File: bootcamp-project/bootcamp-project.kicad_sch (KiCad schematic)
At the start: 17 parts, among them J3 FTDI, SW1 SW_Push, U1 ATmega328P-A, Y1 16MHz

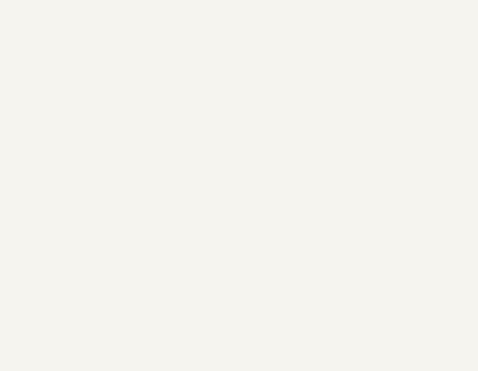
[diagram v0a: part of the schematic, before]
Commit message: lib: fix power flag, foot: add jumpers
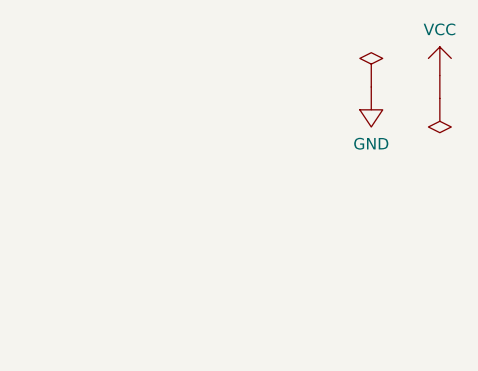
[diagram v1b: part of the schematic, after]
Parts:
- added U2, U3: ~, symbol bootcamp00:POWER_FLAG

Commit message: lib: fix schematic with power flags
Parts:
- added U10, U11, U12, U13, U4, U5, U6, U7, U8, U9: ~, symbol bootcamp00:POWER_FLAG
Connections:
- net RAW: now also U2.1
- net at U1.18 (AVCC), U1.4 (VCC): now also U1.6, U10.1
- net at U1.3 (GND): now also U1.21, U1.5, U13.1
- net at C3.0: now also U9.1
- net at R3.0: now also U4.1
- net at D1.1: now also U6.1
- net at C1.1, C2.1, Y1.2: now also U11.1
- net at Y1.4: now also U12.1
- net at C4.0: now also U5.1
- net at C6.1: now also U8.1
- net at R2.1: now also U3.1
- net at C7.1: now also U7.1

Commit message: sche: update schematic'
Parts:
- C1, C2, C3, C4, C6, C7: footprint (none) -> Library:marge_capacitor
- D1, D2: footprint (none) -> Library:marge_led
- J1: footprint (none) -> Library:JUMPER_12_J1
- J2: footprint (none) -> Library:JUMPER_12_J2
- J3: footprint (none) -> Library:JUMPER_FDTI
- R1, R2, R3: footprint (none) -> Library:marge_resistor
- SW1: footprint (none) -> Library:SWITCH_SW
- U1: footprint (none) -> Library:ATMEGA328p
- Y1: footprint (none) -> Library:QUARTZ_16MHz
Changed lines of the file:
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@@
 			)
 		)
-		(property "Footprint" ""
+		(property "Footprint" "Library:ATMEGA328p"
 			(at 81.28 177.8 0)
 			(effects
@@
 			)
 		)
-		(property "Footprint" ""
+		(property "Footprint" "Library:marge_capacitor"
 			(at 40.64 104.14 0)
 			(effects
@@
 			)
 		)
-		(property "Footprint" ""
+		(property "Footprint" "Library:marge_resistor"
 			(at 205.74 43.18 0)
 			(effects
@@
 			)
 		)
-		(property "Footprint" ""
+		(property "Footprint" "Library:marge_led"
 			(at 135.89 44.45 0)
 			(effects
@@
 	)
 	(symbol
-		(lib_name "POWER_FLAG_2")
 		(lib_id "bootcamp00:POWER_FLAG")
 		(at 205.74 36.83 90)
@@
 			)
 		)
-		(property "Footprint" ""
+		(property "Footprint" "Library:QUARTZ_16MHz"
 			(at 106.68 130.81 0)
 			(effects
@@
 			)
 		)
-		(property "Footprint" ""
+		(property "Footprint" "Library:marge_resistor"
 			(at 134.62 31.75 0)
 			(effects
@@
 			)
 		)
-		(property "Footprint" ""
+		(property "Footprint" "Library:marge_capacitor"
 			(at 185.42 48.26 0)
 			(effects
@@
 			)
 		)
-		(property "Footprint" ""
+		(property "Footprint" "Library:marge_capacitor"
 			(at 43.18 39.37 0)
 			(effects
@@
 			)
 		)
-		(property "Footprint" ""
+		(property "Footprint" "Library:marge_capacitor"
 			(at 115.57 134.62 0)
 			(effects
@@
 	)
 	(symbol
-		(lib_name "POWER_FLAG_1")
 		(lib_id "bootcamp00:POWER_FLAG")
 		(at 63.5 52.07 90)
@@
 	)
 	(symbol
-		(lib_name "POWER_FLAG_3")
 		(lib_id "bootcamp00:POWER_FLAG")
 		(at 175.26 53.34 270)
@@
 			)
 		)
-		(property "Footprint" ""
+		(property "Footprint" "Library:marge_resistor"
 			(at 63.5 45.72 0)
 			(effects
@@
 	)
 	(symbol
-		(lib_name "POWER_FLAG_4")
 		(lib_id "bootcamp00:POWER_FLAG")
 		(at 134.62 50.8 90)
@@
 	)
 	(symbol
-		(lib_name "POWER_FLAG_5")
 		(lib_id "bootcamp00:POWER_FLAG")
 		(at 48.26 43.18 0)
@@
 	)
 	(symbol
-		(lib_name "POWER_FLAG_10")
 		(lib_id "bootcamp00:POWER_FLAG")
 		(at 100.33 129.54 0)
@@
 	)
 	(symbol
-		(lib_name "POWER_FLAG_6")
 		(lib_id "bootcamp00:POWER_FLAG")
 		(at 38.1 43.18 0)
@@
 			)
 		)
-		(property "Footprint" ""
+		(property "Footprint" "Library:SWITCH_SW"
 			(at 194.31 45.72 0)
 			(effects
@@
 			)
 		)
-		(property "Footprint" ""
+		(property "Footprint" "Library:marge_capacitor"
 			(at 53.34 39.37 0)
 			(effects
@@
 			)
 		)
-		(property "Footprint" ""
+		(property "Footprint" "Library:JUMPER_12_J1"
 			(at 152.4 107.95 0)
 			(effects
@@
 			)
 		)
-		(property "Footprint" ""
+		(property "Footprint" "Library:JUMPER_FDTI"
 			(at 220.98 114.3 0)
 			(effects
@@
 	)
 	(symbol
-		(lib_name "POWER_FLAG_9")
 		(lib_id "bootcamp00:POWER_FLAG")
 		(at 125.73 129.54 0)
@@
 	)
 	(symbol
-		(lib_name "POWER_FLAG_8")
 		(lib_id "bootcamp00:POWER_FLAG")
 		(at 69.85 95.25 90)
@@
 	)
 	(symbol
-		(lib_name "POWER_FLAG_11")
 		(lib_id "bootcamp00:POWER_FLAG")
 		(at 63.5 180.34 0)
@@
 			)
 		)
-		(property "Footprint" ""
+		(property "Footprint" "Library:marge_led"
 			(at 64.77 39.37 0)
 			(effects
@@
 			)
 		)
-		(property "Footprint" ""
+		(property "Footprint" "Library:JUMPER_12_J2"
 			(at 191.77 107.95 0)
 			(effects
@@
 	)
 	(symbol
-		(lib_name "POWER_FLAG_7")
 		(lib_id "bootcamp00:POWER_FLAG")
 		(at 33.02 104.14 0)
@@
 			)
 		)
-		(property "Footprint" ""
+		(property "Footprint" "Library:marge_capacitor"
 			(at 115.57 119.38 0)
 			(effects

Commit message: foot: fix pad numb
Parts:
- removed U10, U11, U12, U13, U4, U5, U6, U7, U8, U9: ~, symbol bootcamp00:POWER_FLAG
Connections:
- net GND: now also C1.1, C2.1, C4.0, C6.1, C7.1, D1.1, R2.1, U1.21, U1.3 (GND), U1.5, U2.1, Y1.2, Y1.4
- net VCC: now also C3.0, C6.0, C7.0, D2.0, J2.1, R3.0, U1.18 (AVCC), U1.4 (VCC), U1.6, U3.1
- removed net RAW: C6.0, C7.0, D2.0, J2.1, U2.1
- no-connect marks 0 -> 4

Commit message: pcb: remake a clean pcb
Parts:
- removed U2, U3: ~, symbol bootcamp00:POWER_FLAG
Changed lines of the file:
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@@
+	(wire
+		(pts
+			(xy 66.04 96.52) (xy 69.85 96.52)
+		)
+		(stroke
+			(width 0)
+			(type default)
+		)
+	)
 	(wire
 		(pts
@@
 		(pts
 			(xy 66.04 97.79) (xy 66.04 96.52)
-		)
-		(stroke
-			(width 0)
-			(type default)
-		)
-	)
-	(wire
-		(pts
-			(xy 66.04 96.52) (xy 69.85 96.52)
 		)
 		(stroke
@@
 	)
 	(symbol
+		(lib_id "bootcamp00:VCC")
+		(at 34.29 96.52 0)
+		(unit 1)
+		(exclude_from_sim no)
+		(in_bom yes)
+		(on_board yes)
+		(dnp no)
+		(fields_autoplaced yes)
+		(property "Reference" "#PWR1"
+			(at 34.29 96.52 0)
+			(effects
+				(font
+					(size 1.27 1.27)
+				)
+				(hide yes)
+			)
+		)
+		(property "Value" "VCC"
+			(at 34.29 96.52 0)
+			(effects
+				(font
+					(size 1.27 1.27)
+				)
+			)
+		)
+		(property "Footprint" ""
+			(at 34.29 96.52 0)
+			(effects
+				(font
+					(size 1.27 1.27)
+				)
+				(hide yes)
+			)
+		)
+		(property "Datasheet" ""
+			(at 34.29 96.52 0)
+			(effects
+				(font
+					(size 1.27 1.27)
+				)
+				(hide yes)
+			)
+		)
+		(property "Description" ""
+			(at 34.29 96.52 0)
+			(effects
+				(font
+					(size 1.27 1.27)
+				)
+				(hide yes)
+			)
+		)
+		(pin "0"
+		)
+		(instances
+			(project "bootcamp-project"
+				(path "/48b202d4-8288-4251-bc30-d77995558abc"
+					(reference "#PWR1")
+					(unit 1)
+				)
+			)
+		)
+	)
+	(symbol
 		(lib_id "bootcamp00:POWER_FLAG")
 		(at 63.5 181.61 0)
@@
 		(dnp no)
 		(fields_autoplaced yes)
-		(property "Reference" "U2"
-			(at 63.5 181.61 0)
+		(property "Reference" "#PWR13"
+			(at 62.23 186.436 0)
 			(effects
 				(font
@@
 		)
 		(property "Value" "~"
-			(at 64.77 184.7849 0)
-			(effects
-				(font
-					(size 1.27 1.27)
-				)
-				(justify left)
+			(at 62.23 187.96 0)
+			(effects
+				(font
+					(size 1.27 1.27)
+				)
 				(hide yes)
 			)
@@
 			)
 		)
-		(pin "1"
+		(pin "0"
 		)
 		(instances
 			(project ""
 				(path "/48b202d4-8288-4251-bc30-d77995558abc"
-					(reference "U2")
-					(unit 1)
-				)
-			)
-		)
-	)
-	(symbol
-		(lib_id "bootcamp00:VCC")
-		(at 34.29 96.52 0)
-		(unit 1)
-		(exclude_from_sim no)
-		(in_bom yes)
-		(on_board yes)
-		(dnp no)
-		(fields_autoplaced yes)
-		(property "Reference" "#PWR1"
-			(at 34.29 96.52 0)
-			(effects
-				(font
-					(size 1.27 1.27)
-				)
-				(hide yes)
-			)
-		)
-		(property "Value" "VCC"
-			(at 34.29 96.52 0)
-			(effects
-				(font
-					(size 1.27 1.27)
-				)
-			)
-		)
-		(property "Footprint" ""
-			(at 34.29 96.52 0)
-			(effects
-				(font
-					(size 1.27 1.27)
-				)
-				(hide yes)
-			)
-		)
-		(property "Datasheet" ""
-			(at 34.29 96.52 0)
-			(effects
-				(font
-					(size 1.27 1.27)
-				)
-				(hide yes)
-			)
-		)
-		(property "Description" ""
-			(at 34.29 96.52 0)
-			(effects
-				(font
-					(size 1.27 1.27)
-				)
-				(hide yes)
-			)
-		)
-		(pin "0"
-		)
-		(instances
-			(project "bootcamp-project"
-				(path "/48b202d4-8288-4251-bc30-d77995558abc"
-					(reference "#PWR1")
+					(reference "#PWR13")
 					(unit 1)
 				)
@@
 	)
 	(symbol
+		(lib_name "POWER_FLAG_1")
+		(lib_id "bootcamp00:POWER_FLAG")
+		(at 68.58 96.52 180)
+		(unit 1)
+		(exclude_from_sim no)
+		(in_bom yes)
+		(on_board yes)
+		(dnp no)
+		(fields_autoplaced yes)
+		(property "Reference" "#PWR14"
+			(at 69.85 91.694 0)
+			(effects
+				(font
+					(size 1.27 1.27)
+				)
+				(hide yes)
+			)
+		)
+		(property "Value" "~"
+			(at 69.85 90.17 0)
+			(effects
+				(font
+					(size 1.27 1.27)
+				)
+				(hide yes)
+			)
+		)
+		(property "Footprint" ""
+			(at 68.58 96.52 0)
+			(effects
+				(font
+					(size 1.27 1.27)
+				)
+				(hide yes)
+			)
+		)
+		(property "Datasheet" ""
+			(at 68.58 96.52 0)
+			(effects
+				(font
+					(size 1.27 1.27)
+				)
+				(hide yes)
+			)
+		)
+		(property "Description" ""
+			(at 68.58 96.52 0)
+			(effects
+				(font
+					(size 1.27 1.27)
+				)
+				(hide yes)
+			)
+		)
+		(pin "0"
+		)
+		(instances
+			(project ""
+				(path "/48b202d4-8288-4251-bc30-d77995558abc"
+					(reference "#PWR14")
+					(unit 1)
+				)
+			)
+		)
+	)
+	(symbol
 		(lib_id "bootcamp00:QUARTZ")
 		(at 106.68 130.81 0)
@@
 					(unit 1)
 				)
-			)
-		)
-	)
-	(symbol
-		(lib_name "POWER_FLAG_1")
-		(lib_id "bootcamp00:POWER_FLAG")
-		(at 68.58 96.52 180)
-		(unit 1)
-		(exclude_from_sim no)
-		(in_bom yes)
-		(on_board yes)
-		(dnp no)
-		(fields_autoplaced yes)
-		(property "Reference" "U3"
-			(at 68.58 96.52 0)
-			(effects
-				(font
-					(size 1.27 1.27)
-				)
-				(hide yes)
-			)
-		)
-		(property "Value" "~"
-			(at 72.39 93.3449 0)
-			(effects
-				(font
-					(size 1.27 1.27)
-				)
-				(justify right)
-				(hide yes)
-			)
-		)
-		(property "Footprint" ""
-			(at 68.58 96.52 0)
-			(effects
-				(font
-					(size 1.27 1.27)
-				)
-				(hide yes)
-			)
-		)
-		(property "Datasheet" ""
-			(at 68.58 96.52 0)
-			(effects
-				(font
-					(size 1.27 1.27)
-				)
-				(hide yes)
-			)
-		)
-		(property "Description" ""
-			(at 68.58 96.52 0)
-			(effects
-				(font
-					(size 1.27 1.27)
-				)
-				(hide yes)
-			)
-		)
-		(pin "1"
-		)
-		(instances
-			(project ""
-				(path "/48b202d4-8288-4251-bc30-d77995558abc"
-					(reference "U3")
-					(unit 1)
-				)
